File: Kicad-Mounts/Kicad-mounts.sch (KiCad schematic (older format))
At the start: 8 parts, among them P1 CONN_10, P2 CONN_10, P3 CONN_6X2, P4 CONN_3, P5 CONN_3, P6 CONN_3

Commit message: Modification of boards after checking. Addition of other LED types to LED mount board.
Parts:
- D1: footprint Photodiode:VSMY2850 -> Photodiode:LED-mount
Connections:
- no-connect marks 2 -> 1
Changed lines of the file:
@@
 LIBS:contrib
 LIBS:valves
-LIBS:RF_OEM_Parts
 LIBS:Kicad-mounts-cache
 EELAYER 24 0
@@
 F 0 "D1" H 8050 5300 50  0000 C CNN
 F 1 "LED" H 8050 5100 50  0000 C CNN
-F 2 "Photodiode:VSMY2850" H 8050 5200 60  0001 C CNN
+F 2 "Photodiode:LED-mount" H 8050 5200 60  0001 C CNN
 F 3 "" H 8050 5200 60  0000 C CNN
 	1    8050 5200
@@
 Text Label 4250 5200 0    60   ~ 0
 RTS
-NoConn ~ 5200 5150
+$Comp
+L GND #PWR?
+U 1 1 53FEF8A0
+P 5200 5150
+F 0 "#PWR?" H 5200 5150 30  0001 C CNN
+F 1 "GND" H 5200 5080 30  0001 C CNN
+F 2 "" H 5200 5150 60  0000 C CNN
+F 3 "" H 5200 5150 60  0000 C CNN
+	1    5200 5150
+	0    1    1    0
+$EndComp
 $EndSCHEMATC

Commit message: Change schematic symbols for connectors as Kicad, inexplicably, removed them.
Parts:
- P1, P2: symbol CONN_10 -> CONN_01X10
- P3: symbol CONN_6X2 -> CONN_02X06
- P4, P5, P6: symbol CONN_3 -> CONN_01X03
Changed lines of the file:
@@
 LIBS:contrib
 LIBS:valves
-LIBS:Kicad-mounts-cache
+LIBS:KB1LQC
+LIBS:MiscellaneousDevices
+LIBS:Sensors
+LIBS:RF_OEM_Parts
 EELAYER 24 0
 EELAYER END
@@
 $EndComp
 $Comp
-L CONN_3 P4
+L CONN_01X03 P4
 U 1 1 53F674B3
-P 5550 4750
-F 0 "P4" V 5500 4750 50  0000 C CNN
-F 1 "CONN_3" V 5600 4750 40  0000 C CNN
-F 2 "Photodiode:pin_header_2mm_1x3" H 5550 4750 60  0001 C CNN
-F 3 "" H 5550 4750 60  0000 C CNN
-	1    5550 4750
-	1    0    0    -1
-$EndComp
-$Comp
-L CONN_3 P5
+P 5400 4750
+F 0 "P4" V 5350 4750 50  0000 C CNN
+F 1 "CONN_3" V 5450 4750 40  0000 C CNN
+F 2 "Photodiode:pin_header_2mm_1x3" H 5400 4750 60  0001 C CNN
+F 3 "" H 5400 4750 60  0000 C CNN
+	1    5400 4750
+	1    0    0    -1
+$EndComp
+$Comp
+L CONN_01X03 P5
 U 1 1 53F6753C
-P 5550 5250
-F 0 "P5" V 5500 5250 50  0000 C CNN
-F 1 "CONN_3" V 5600 5250 40  0000 C CNN
-F 2 "Photodiode:pin_header_2mm_1x3" H 5550 5250 60  0001 C CNN
-F 3 "" H 5550 5250 60  0000 C CNN
-	1    5550 5250
-	1    0    0    -1
-$EndComp
-$Comp
-L CONN_6X2 P3
+P 5400 5250
+F 0 "P5" V 5350 5250 50  0000 C CNN
+F 1 "CONN_3" V 5450 5250 40  0000 C CNN
+F 2 "Photodiode:pin_header_2mm_1x3" H 5400 5250 60  0001 C CNN
+F 3 "" H 5400 5250 60  0000 C CNN
+	1    5400 5250
+	1    0    0    -1
+$EndComp
+$Comp
+L CONN_02X06 P3
 U 1 1 53F67592
-P 3850 5050
-F 0 "P3" H 3850 5400 60  0000 C CNN
-F 1 "CONN_6X2" V 3850 5050 60  0000 C CNN
-F 2 "Photodiode:pin_header_2mm_2x6" H 3850 5050 60  0001 C CNN
-F 3 "" H 3850 5050 60  0000 C CNN
-	1    3850 5050
-	1    0    0    -1
-$EndComp
-$Comp
-L CONN_10 P2
+P 3700 5050
+F 0 "P3" H 3700 5400 60  0000 C CNN
+F 1 "CONN_6X2" V 3700 5050 60  0000 C CNN
+F 2 "Photodiode:pin_header_2mm_2x6" H 3700 5050 60  0001 C CNN
+F 3 "" H 3700 5050 60  0000 C CNN
+	1    3700 5050
+	1    0    0    -1
+$EndComp
+$Comp
+L CONN_01X10 P2
 U 1 1 53F675C9
-P 6350 3850
-F 0 "P2" V 6300 3850 60  0000 C CNN
-F 1 "CONN_10" V 6400 3850 60  0000 C CNN
-F 2 "Connect:SIL-10" H 6350 3850 60  0001 C CNN
-F 3 "" H 6350 3850 60  0000 C CNN
-	1    6350 3850
-	1    0    0    -1
-$EndComp
-$Comp
-L CONN_10 P1
+P 6200 3850
+F 0 "P2" V 6150 3850 60  0000 C CNN
+F 1 "CONN_10" V 6250 3850 60  0000 C CNN
+F 2 "Connect:SIL-10" H 6200 3850 60  0001 C CNN
+F 3 "" H 6200 3850 60  0000 C CNN
+	1    6200 3850
+	1    0    0    -1
+$EndComp
+$Comp
+L CONN_01X10 P1
 U 1 1 53F6774F
-P 1850 3850
-F 0 "P1" V 1800 3850 60  0000 C CNN
-F 1 "CONN_10" V 1900 3850 60  0000 C CNN
-F 2 "Connect:SIL-10" H 1850 3850 60  0001 C CNN
-F 3 "" H 1850 3850 60  0000 C CNN
-	1    1850 3850
+P 2000 3850
+F 0 "P1" V 1950 3850 60  0000 C CNN
+F 1 "CONN_10" V 2050 3850 60  0000 C CNN
+F 2 "Connect:SIL-10" H 2000 3850 60  0001 C CNN
+F 3 "" H 2000 3850 60  0000 C CNN
+	1    2000 3850
 	-1   0    0    -1
 $EndComp
 $Comp
-L CONN_3 P6
+L CONN_01X03 P6
 U 1 1 53F679DA
-P 9100 5200
-F 0 "P6" V 9050 5200 50  0000 C CNN
-F 1 "CONN_3" V 9150 5200 40  0000 C CNN
-F 2 "Connect:SIL-3" H 9100 5200 60  0001 C CNN
-F 3 "" H 9100 5200 60  0000 C CNN
-	1    9100 5200
+P 8950 5200
+F 0 "P6" V 8900 5200 50  0000 C CNN
+F 1 "CONN_3" V 9000 5200 40  0000 C CNN
+F 2 "Connect:SIL-3" H 8950 5200 60  0001 C CNN
+F 3 "" H 8950 5200 60  0000 C CNN
+	1    8950 5200
 	1    0    0    -1
 $EndComp
@@
 Text Label 3450 4900 2    60   ~ 0
 Bootloader
-Text Label 4250 4900 0    60   ~ 0
+Text Label 3950 4900 0    60   ~ 0
 VBatt
 Text Label 3450 5000 2    60   ~ 0
 Reset
-Text Label 4250 5000 0    60   ~ 0
+Text Label 3950 5000 0    60   ~ 0
 XBee-Reset
 Text Label 3450 5100 2    60   ~ 0
 Rx
-Text Label 4250 5100 0    60   ~ 0
+Text Label 3950 5100 0    60   ~ 0
 Sleep_Rq
 Text Label 3450 5200 2    60   ~ 0
 On/Sleep
-Text Label 4250 5300 0    60   ~ 0
+Text Label 3950 5300 0    60   ~ 0
 Tx
 $Comp
@@
 L VCC #PWR02
 U 1 1 53F6854B
-P 4250 4800
-F 0 "#PWR02" H 4250 4900 30  0001 C CNN
-F 1 "VCC" V 4250 4950 30  0000 C CNN
-F 2 "" H 4250 4800 60  0000 C CNN
-F 3 "" H 4250 4800 60  0000 C CNN
-	1    4250 4800
+P 3950 4800
+F 0 "#PWR02" H 3950 4900 30  0001 C CNN
+F 1 "VCC" V 3950 4950 30  0000 C CNN
+F 2 "" H 3950 4800 60  0000 C CNN
+F 3 "" H 3950 4800 60  0000 C CNN
+	1    3950 4800
 	0    1    1    0
 $EndComp
@@
 L PWR_FLAG #FLG05
 U 1 1 53F68599
-P 4250 4800
-F 0 "#FLG05" H 4250 4895 30  0001 C CNN
-F 1 "PWR_FLAG" H 4250 4980 30  0000 C CNN
-F 2 "" H 4250 4800 60  0000 C CNN
-F 3 "" H 4250 4800 60  0000 C CNN
-	1    4250 4800
+P 3950 4800
+F 0 "#FLG05" H 3950 4895 30  0001 C CNN
+F 1 "PWR_FLAG" H 3950 4980 30  0000 C CNN
+F 2 "" H 3950 4800 60  0000 C CNN
+F 3 "" H 3950 4800 60  0000 C CNN
+	1    3950 4800
 	1    0    0    -1
 $EndComp
@@
 $EndComp
 NoConn ~ 3450 4800
-Text Label 4250 5200 0    60   ~ 0
+Text Label 3950 5200 0    60   ~ 0
 RTS
 $Comp

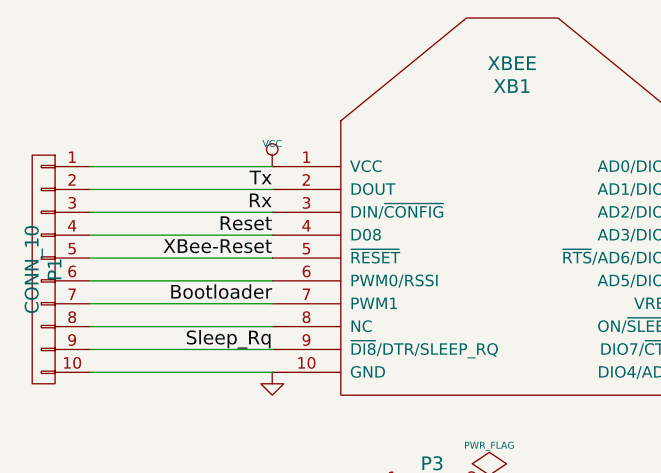
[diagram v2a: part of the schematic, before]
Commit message: Swap over Tx and Rx
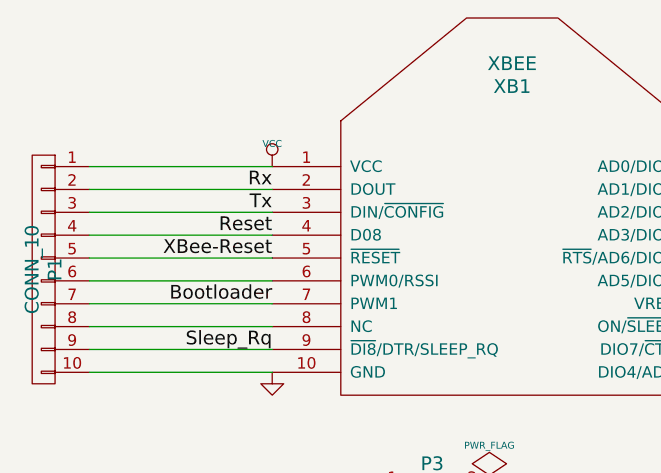
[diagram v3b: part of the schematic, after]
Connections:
- net Rx: now also P1.2 (P2), XB1.2 (DOUT); no longer P1.3 (P3), XB1.3 (DIN/~CONFIG)
- net Tx: now also P1.3 (P3), XB1.3 (DIN/~CONFIG); no longer P1.2 (P2), XB1.2 (DOUT)
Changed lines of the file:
@@
 Text Label 5100 4100 0    60   ~ 0
 On/Sleep
+Text Label 3000 3600 2    60   ~ 0
+Tx
 Text Label 3000 3500 2    60   ~ 0
-Tx
-Text Label 3000 3600 2    60   ~ 0
 Rx
 Text Label 5200 5250 2    60   ~ 0

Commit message: Change PCBs to move XBee regulator and caps to the mount board. Change Vcc on mount board to take full battery voltage.
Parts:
- added C1: 0.47uF, symbol C
- added C2: 0.1uF, symbol C
- added C3: 10uF, symbol CAPAPOL
- added U2: TPS77033, symbol TPS77033
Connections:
- net labels added: V3
- wire segments 24 -> 26
- no-connect marks 1 -> 2
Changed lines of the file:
@@
 LIBS:Sensors
 LIBS:RF_OEM_Parts
+LIBS:Kicad-mounts-cache
 EELAYER 24 0
 EELAYER END
@@
 F 3 "" H 3000 4300 60  0000 C CNN
 	1    3000 4300
-	1    0    0    -1
-$EndComp
-$Comp
-L VCC #PWR04
-U 1 1 53F689F2
-P 3000 3400
-F 0 "#PWR04" H 3000 3500 30  0001 C CNN
-F 1 "VCC" H 3000 3500 30  0000 C CNN
-F 2 "" H 3000 3400 60  0000 C CNN
-F 3 "" H 3000 3400 60  0000 C CNN
-	1    3000 3400
 	1    0    0    -1
 $EndComp
@@
 Connection ~ 8750 5300
 $Comp
-L PWR_FLAG #FLG05
+L PWR_FLAG #FLG04
 U 1 1 53F68599
 P 3950 4800
-F 0 "#FLG05" H 3950 4895 30  0001 C CNN
+F 0 "#FLG04" H 3950 4895 30  0001 C CNN
 F 1 "PWR_FLAG" H 3950 4980 30  0000 C CNN
 F 2 "" H 3950 4800 60  0000 C CNN
@@
 $EndComp
 $Comp
-L PWR_FLAG #FLG06
+L PWR_FLAG #FLG05
 U 1 1 53F685B5
 P 3450 5300
-F 0 "#FLG06" H 3450 5395 30  0001 C CNN
+F 0 "#FLG05" H 3450 5395 30  0001 C CNN
 F 1 "PWR_FLAG" H 3450 5480 30  0000 C CNN
 F 2 "" H 3450 5300 60  0000 C CNN
@@
 RTS
 $Comp
-L GND #PWR?
+L GND #PWR06
 U 1 1 53FEF8A0
 P 5200 5150
-F 0 "#PWR?" H 5200 5150 30  0001 C CNN
+F 0 "#PWR06" H 5200 5150 30  0001 C CNN
 F 1 "GND" H 5200 5080 30  0001 C CNN
 F 2 "" H 5200 5150 60  0000 C CNN
@@
 	0    1    1    0
 $EndComp
+$Comp
+L TPS77033 U2
+U 1 1 549A2F0F
+P 3700 6100
+F 0 "U2" H 3850 5704 60  0000 C CNN
+F 1 "TPS77033" H 3700 6300 60  0000 C CNN
+F 2 "" H 3700 6100 60  0000 C CNN
+F 3 "" H 3700 6100 60  0000 C CNN
+	1    3700 6100
+	1    0    0    -1
+$EndComp
+$Comp
+L C C1
+U 1 1 549A30D6
+P 2800 6250
+F 0 "C1" H 2800 6350 40  0000 L CNN
+F 1 "0.47uF" H 2806 6165 40  0000 L CNN
+F 2 "" H 2838 6100 30  0000 C CNN
+F 3 "" H 2800 6250 60  0000 C CNN
+	1    2800 6250
+	1    0    0    -1
+$EndComp
+$Comp
+L C C2
+U 1 1 549A3151
+P 4600 6400
+F 0 "C2" H 4600 6500 40  0000 L CNN
+F 1 "0.1uF" H 4606 6315 40  0000 L CNN
+F 2 "" H 4638 6250 30  0000 C CNN
+F 3 "" H 4600 6400 60  0000 C CNN
+	1    4600 6400
+	1    0    0    -1
+$EndComp
+$Comp
+L CAPAPOL C3
+U 1 1 549A31E1
+P 5000 6400
+F 0 "C3" H 5050 6500 40  0000 L CNN
+F 1 "10uF" H 5050 6300 40  0000 L CNN
+F 2 "" H 5100 6250 30  0000 C CNN
+F 3 "" H 5000 6400 300 0000 C CNN
+	1    5000 6400
+	1    0    0    -1
+$EndComp
+Wire Wire Line
+	2650 6050 3400 6050
+Wire Wire Line
+	4000 6200 5200 6200
+$Comp
+L GND #PWR07
+U 1 1 549A3CE1
+P 3700 6550
+F 0 "#PWR07" H 3700 6550 30  0001 C CNN
+F 1 "GND" H 3700 6480 30  0001 C CNN
+F 2 "" H 3700 6550 60  0000 C CNN
+F 3 "" H 3700 6550 60  0000 C CNN
+	1    3700 6550
+	1    0    0    -1
+$EndComp
+$Comp
+L GND #PWR08
+U 1 1 549A3D0B
+P 4600 6600
+F 0 "#PWR08" H 4600 6600 30  0001 C CNN
+F 1 "GND" H 4600 6530 30  0001 C CNN
+F 2 "" H 4600 6600 60  0000 C CNN
+F 3 "" H 4600 6600 60  0000 C CNN
+	1    4600 6600
+	1    0    0    -1
+$EndComp
+$Comp
+L GND #PWR09
+U 1 1 549A3D2E
+P 5000 6600
+F 0 "#PWR09" H 5000 6600 30  0001 C CNN
+F 1 "GND" H 5000 6530 30  0001 C CNN
+F 2 "" H 5000 6600 60  0000 C CNN
+F 3 "" H 5000 6600 60  0000 C CNN
+	1    5000 6600
+	1    0    0    -1
+$EndComp
+$Comp
+L GND #PWR010
+U 1 1 549A3D51
+P 2800 6450
+F 0 "#PWR010" H 2800 6450 30  0001 C CNN
+F 1 "GND" H 2800 6380 30  0001 C CNN
+F 2 "" H 2800 6450 60  0000 C CNN
+F 3 "" H 2800 6450 60  0000 C CNN
+	1    2800 6450
+	1    0    0    -1
+$EndComp
+NoConn ~ 4000 6050
+$Comp
+L GND #PWR011
+U 1 1 549A3D98
+P 3400 6300
+F 0 "#PWR011" H 3400 6300 30  0001 C CNN
+F 1 "GND" H 3400 6230 30  0001 C CNN
+F 2 "" H 3400 6300 60  0000 C CNN
+F 3 "" H 3400 6300 60  0000 C CNN
+	1    3400 6300
+	0    1    1    0
+$EndComp
+$Comp
+L VCC #PWR012
+U 1 1 549A5134
+P 2650 6050
+F 0 "#PWR012" H 2650 6150 30  0001 C CNN
+F 1 "VCC" V 2650 6200 30  0000 C CNN
+F 2 "" H 2650 6050 60  0000 C CNN
+F 3 "" H 2650 6050 60  0000 C CNN
+	1    2650 6050
+	0    -1   1    0
+$EndComp
+Text Label 3000 3400 2    60   ~ 0
+V3
+Text Label 5200 6200 0    60   ~ 0
+V3
+Connection ~ 5000 6200
+Connection ~ 4600 6200
+Connection ~ 2800 6050
 $EndSCHEMATC

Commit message: Setup of KiCad projects to point to local libraries in repository. Corrections to mounts schematic.
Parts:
- C3: symbol CAPAPOL -> CP
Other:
- moved on the sheet: C1, C2
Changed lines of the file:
@@
 LIBS:Sensors
 LIBS:RF_OEM_Parts
-LIBS:Kicad-mounts-cache
-EELAYER 24 0
+EELAYER 25 0
 EELAYER END
 $Descr A4 11693 8268
@@
 L C C1
 U 1 1 549A30D6
-P 2800 6250
-F 0 "C1" H 2800 6350 40  0000 L CNN
-F 1 "0.47uF" H 2806 6165 40  0000 L CNN
-F 2 "" H 2838 6100 30  0000 C CNN
-F 3 "" H 2800 6250 60  0000 C CNN
-	1    2800 6250
+P 2800 6200
+F 0 "C1" H 2800 6300 40  0000 L CNN
+F 1 "0.47uF" H 2806 6115 40  0000 L CNN
+F 2 "" H 2838 6050 30  0000 C CNN
+F 3 "" H 2800 6200 60  0000 C CNN
+	1    2800 6200
 	1    0    0    -1
 $EndComp
@@
 L C C2
 U 1 1 549A3151
-P 4600 6400
-F 0 "C2" H 4600 6500 40  0000 L CNN
-F 1 "0.1uF" H 4606 6315 40  0000 L CNN
-F 2 "" H 4638 6250 30  0000 C CNN
-F 3 "" H 4600 6400 60  0000 C CNN
-	1    4600 6400
-	1    0    0    -1
-$EndComp
-$Comp
-L CAPAPOL C3
+P 4600 6350
+F 0 "C2" H 4600 6450 40  0000 L CNN
+F 1 "0.1uF" H 4606 6265 40  0000 L CNN
+F 2 "" H 4638 6200 30  0000 C CNN
+F 3 "" H 4600 6350 60  0000 C CNN
+	1    4600 6350
+	1    0    0    -1
+$EndComp
+$Comp
+L CP C3
 U 1 1 549A31E1
-P 5000 6400
-F 0 "C3" H 5050 6500 40  0000 L CNN
-F 1 "10uF" H 5050 6300 40  0000 L CNN
-F 2 "" H 5100 6250 30  0000 C CNN
-F 3 "" H 5000 6400 300 0000 C CNN
-	1    5000 6400
+P 5000 6350
+F 0 "C3" H 5050 6450 40  0000 L CNN
+F 1 "10uF" H 5050 6250 40  0000 L CNN
+F 2 "" H 5100 6200 30  0000 C CNN
+F 3 "" H 5000 6350 300 0000 C CNN
+	1    5000 6350
 	1    0    0    -1
 $EndComp
@@
 L GND #PWR08
 U 1 1 549A3D0B
-P 4600 6600
-F 0 "#PWR08" H 4600 6600 30  0001 C CNN
-F 1 "GND" H 4600 6530 30  0001 C CNN
-F 2 "" H 4600 6600 60  0000 C CNN
-F 3 "" H 4600 6600 60  0000 C CNN
-	1    4600 6600
+P 4600 6500
+F 0 "#PWR08" H 4600 6500 30  0001 C CNN
+F 1 "GND" H 4600 6430 30  0001 C CNN
+F 2 "" H 4600 6500 60  0000 C CNN
+F 3 "" H 4600 6500 60  0000 C CNN
+	1    4600 6500
 	1    0    0    -1
 $EndComp
@@
 L GND #PWR09
 U 1 1 549A3D2E
-P 5000 6600
-F 0 "#PWR09" H 5000 6600 30  0001 C CNN
-F 1 "GND" H 5000 6530 30  0001 C CNN
-F 2 "" H 5000 6600 60  0000 C CNN
-F 3 "" H 5000 6600 60  0000 C CNN
-	1    5000 6600
+P 5000 6500
+F 0 "#PWR09" H 5000 6500 30  0001 C CNN
+F 1 "GND" H 5000 6430 30  0001 C CNN
+F 2 "" H 5000 6500 60  0000 C CNN
+F 3 "" H 5000 6500 60  0000 C CNN
+	1    5000 6500
 	1    0    0    -1
 $EndComp
@@
 L GND #PWR010
 U 1 1 549A3D51
-P 2800 6450
-F 0 "#PWR010" H 2800 6450 30  0001 C CNN
-F 1 "GND" H 2800 6380 30  0001 C CNN
-F 2 "" H 2800 6450 60  0000 C CNN
-F 3 "" H 2800 6450 60  0000 C CNN
-	1    2800 6450
-	1    0    0    -1
-$EndComp
+P 2800 6350
+F 0 "#PWR010" H 2800 6350 30  0001 C CNN
+F 1 "GND" H 2800 6280 30  0001 C CNN
+F 2 "" H 2800 6350 60  0000 C CNN
+F 3 "" H 2800 6350 60  0000 C CNN
+	1    2800 6350
+	1    0    0    -1
+$EndComp

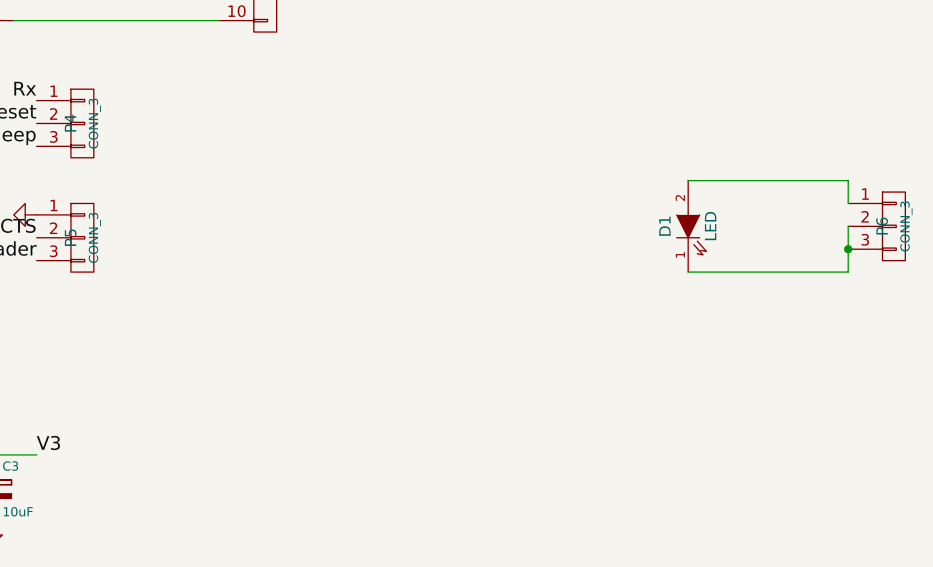
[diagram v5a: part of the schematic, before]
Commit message: Modified both Main and Mounts PCBs to have all footprints in the local library Photodiode.pretty. Saved footprints already in the PCB hopefully avoiding invalidating the PCB in future. Minor changes to schematic and KICAD_SETUP.md
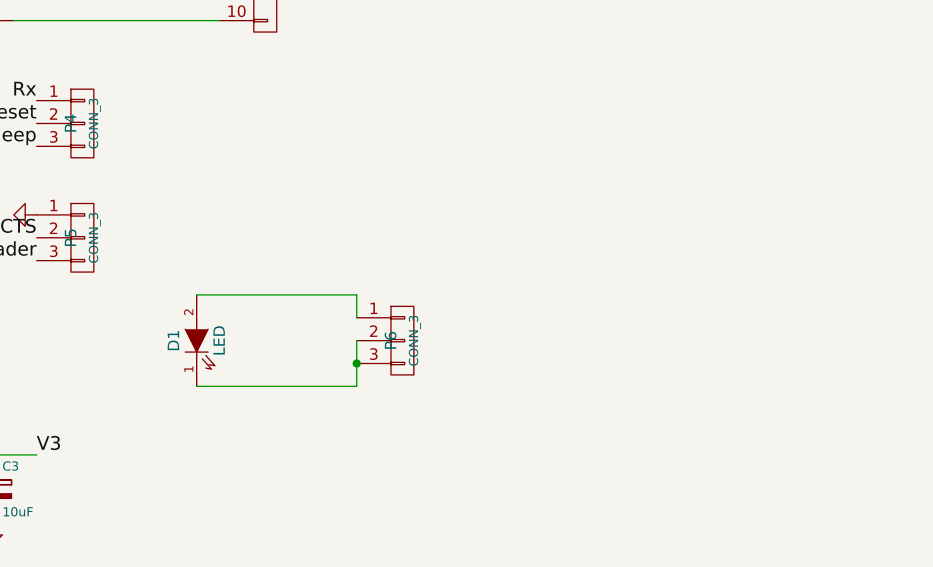
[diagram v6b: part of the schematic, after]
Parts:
- C1, C2: footprint (none) -> Photodiode:SMD-0603_c
- C3: footprint (none) -> Photodiode:SMD-1206_Pol
- P1, P2: footprint Connect:SIL-10 -> Photodiode:SIL-10
- P6: footprint Connect:SIL-3 -> Photodiode:SIL-3
- U2: footprint (none) -> Photodiode:SOT-23-5
- XB1: footprint Imciner:XBee -> Photodiode:XBee
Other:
- moved on the sheet: D1, P6
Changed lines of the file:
@@
 LIBS:memory
 LIBS:xilinx
-LIBS:special
 LIBS:microcontrollers
 LIBS:dsp
@@
 LIBS:Sensors
 LIBS:RF_OEM_Parts
+LIBS:Kicad-mounts-cache
 EELAYER 25 0
 EELAYER END
@@
 F 0 "XB1" H 4050 4650 60  0000 C CNN
 F 1 "XBEE" H 4050 4750 60  0000 C CNN
-F 2 "Imciner:XBee" H 4050 3850 60  0001 C CNN
+F 2 "Photodiode:XBee" H 4050 3850 60  0001 C CNN
 F 3 "" H 4050 3850 60  0000 C CNN
 	1    4050 3850
@@
 F 0 "P2" V 6150 3850 60  0000 C CNN
 F 1 "CONN_10" V 6250 3850 60  0000 C CNN
-F 2 "Connect:SIL-10" H 6200 3850 60  0001 C CNN
+F 2 "Photodiode:SIL-10" H 6200 3850 60  0001 C CNN
 F 3 "" H 6200 3850 60  0000 C CNN
 	1    6200 3850
@@
 F 0 "P1" V 1950 3850 60  0000 C CNN
 F 1 "CONN_10" V 2050 3850 60  0000 C CNN
-F 2 "Connect:SIL-10" H 2000 3850 60  0001 C CNN
+F 2 "Photodiode:SIL-10" H 2000 3850 60  0001 C CNN
 F 3 "" H 2000 3850 60  0000 C CNN
 	1    2000 3850
@@
 L CONN_01X03 P6
 U 1 1 53F679DA
-P 8950 5200
-F 0 "P6" V 8900 5200 50  0000 C CNN
-F 1 "CONN_3" V 9000 5200 40  0000 C CNN
-F 2 "Connect:SIL-3" H 8950 5200 60  0001 C CNN
-F 3 "" H 8950 5200 60  0000 C CNN
-	1    8950 5200
+P 6800 5700
+F 0 "P6" V 6750 5700 50  0000 C CNN
+F 1 "CONN_3" V 6850 5700 40  0000 C CNN
+F 2 "Photodiode:SIL-3" H 6800 5700 60  0001 C CNN
+F 3 "" H 6800 5700 60  0000 C CNN
+	1    6800 5700
 	1    0    0    -1
 $EndComp
@@
 L LED D1
 U 1 1 53F67A70
-P 8050 5200
-F 0 "D1" H 8050 5300 50  0000 C CNN
-F 1 "LED" H 8050 5100 50  0000 C CNN
-F 2 "Photodiode:LED-mount" H 8050 5200 60  0001 C CNN
-F 3 "" H 8050 5200 60  0000 C CNN
-	1    8050 5200
+P 5900 5700
+F 0 "D1" H 5900 5800 50  0000 C CNN
+F 1 "LED" H 5900 5600 50  0000 C CNN
+F 2 "Photodiode:LED-mount" H 5900 5700 60  0001 C CNN
+F 3 "" H 5900 5700 60  0000 C CNN
+	1    5900 5700
 	0    -1   -1   0
 $EndComp
 Wire Wire Line
-	8750 5100 8750 5000
-Wire Wire Line
-	8750 5000 8050 5000
-Wire Wire Line
-	8750 5200 8750 5400
-Wire Wire Line
-	8750 5400 8050 5400
+	6600 5600 6600 5500
+Wire Wire Line
+	6600 5500 5900 5500
+Wire Wire Line
+	6600 5700 6600 5900
+Wire Wire Line
+	6600 5900 5900 5900
 Wire Wire Line
 	2200 3400 3000 3400
@@
 Text Label 5100 3500 0    60   ~ 0
 VBatt
-Connection ~ 8750 5300
+Connection ~ 6600 5800
 $Comp
 L PWR_FLAG #FLG04
@@
 F 0 "U2" H 3850 5704 60  0000 C CNN
 F 1 "TPS77033" H 3700 6300 60  0000 C CNN
-F 2 "" H 3700 6100 60  0000 C CNN
+F 2 "Photodiode:SOT-23-5" H 3700 6100 60  0001 C CNN
 F 3 "" H 3700 6100 60  0000 C CNN
 	1    3700 6100
@@
 F 0 "C1" H 2800 6300 40  0000 L CNN
 F 1 "0.47uF" H 2806 6115 40  0000 L CNN
-F 2 "" H 2838 6050 30  0000 C CNN
+F 2 "Photodiode:SMD-0603_c" H 2838 6050 30  0001 C CNN
 F 3 "" H 2800 6200 60  0000 C CNN
 	1    2800 6200
@@
 F 0 "C2" H 4600 6450 40  0000 L CNN
 F 1 "0.1uF" H 4606 6265 40  0000 L CNN
-F 2 "" H 4638 6200 30  0000 C CNN
+F 2 "Photodiode:SMD-0603_c" H 4638 6200 30  0001 C CNN
 F 3 "" H 4600 6350 60  0000 C CNN
 	1    4600 6350
@@
 F 0 "C3" H 5050 6450 40  0000 L CNN
 F 1 "10uF" H 5050 6250 40  0000 L CNN
-F 2 "" H 5100 6200 30  0000 C CNN
+F 2 "Photodiode:SMD-1206_Pol" H 5100 6200 30  0001 C CNN
 F 3 "" H 5000 6350 300 0000 C CNN
 	1    5000 6350

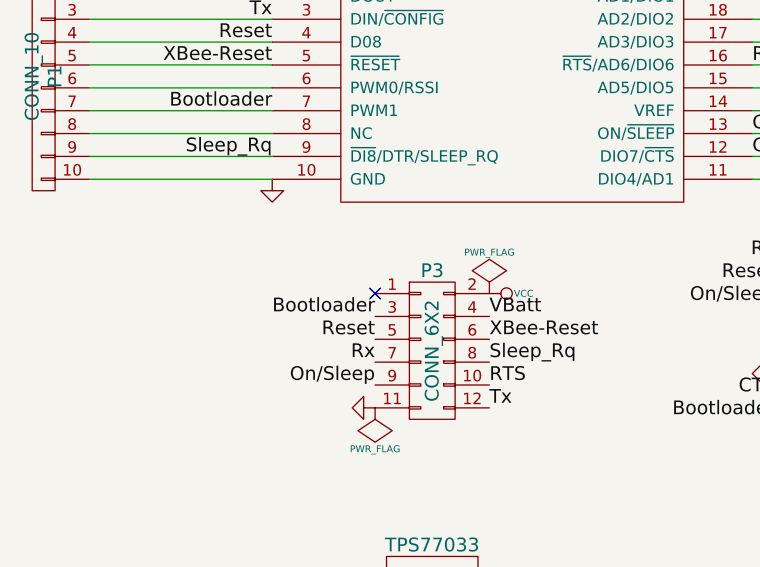
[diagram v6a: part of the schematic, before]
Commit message: Change mount board to rotate XBee sideways and keep dual row connector only
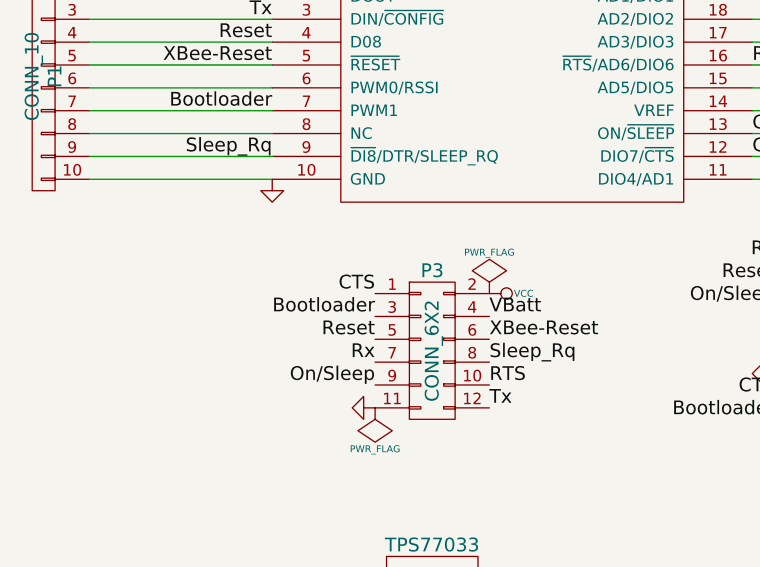
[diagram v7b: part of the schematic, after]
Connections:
- net CTS: now also P3.1 (P1)
- no-connect marks 2 -> 1
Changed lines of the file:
@@
 Text Label 3000 3500 2    60   ~ 0
 Rx
-Text Label 5200 5250 2    60   ~ 0
+Text Label 3450 4800 2    60   ~ 0
 CTS
 Text Label 5100 3800 0    60   ~ 0
@@
 	-1   0    0    1
 $EndComp
-NoConn ~ 3450 4800
 Text Label 3950 5200 0    60   ~ 0
 RTS
@@
 Connection ~ 4600 6200
 Connection ~ 2800 6050
+Text Label 5200 5250 2    60   ~ 0
+CTS
 $EndSCHEMATC
